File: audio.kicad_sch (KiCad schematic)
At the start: 18 parts, among them U13 CMM4030D, U15 MAX98357A

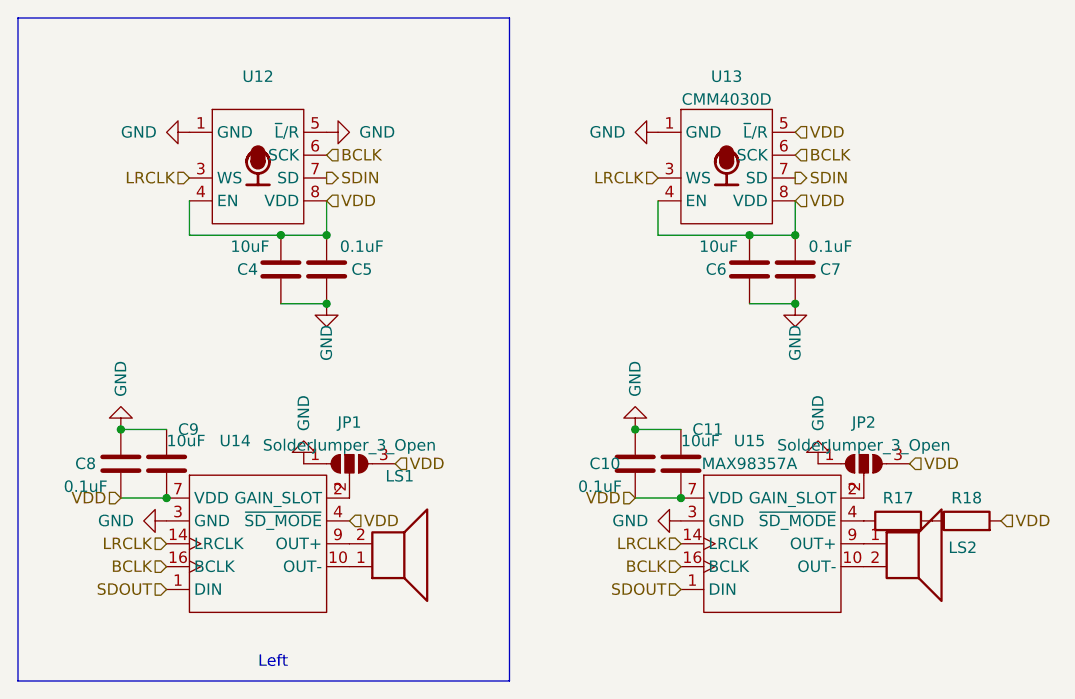
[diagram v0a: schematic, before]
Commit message: fully routed
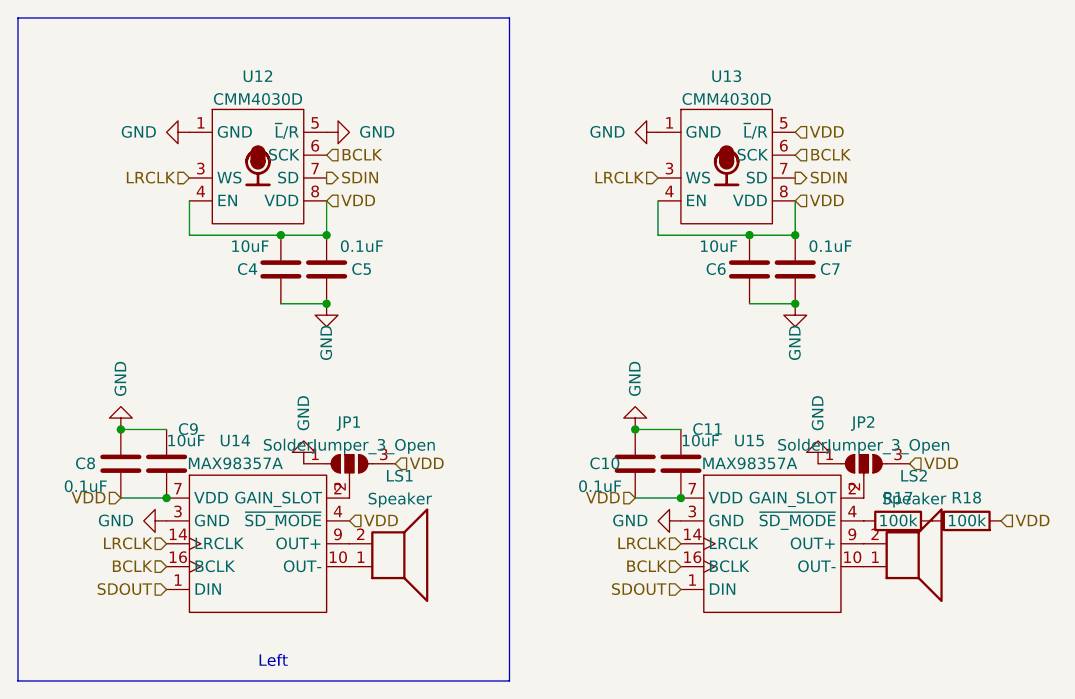
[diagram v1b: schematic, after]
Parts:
- JP1, JP2: footprint (none) -> Jumper:SolderJumper-3_P1.3mm_Open_RoundedPad1.0x1.5mm
- LS1, LS2: value (none) -> Speaker; footprint (none) -> misc:CMS1609
- R17, R18: value (none) -> 100k; footprint (none) -> Resistor_SMD:R_0603_1608Metric
- U12: value (none) -> CMM4030D
- U14: value (none) -> MAX98357A
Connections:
- net at LS2.1: now also U15.10 (OUT-); no longer U15.9 (OUT+)
- net at LS2.2: now also U15.9 (OUT+); no longer U15.10 (OUT-)
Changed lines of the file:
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@@
     (in_bom yes) (on_board yes)
     (property "Reference" "R18" (id 0) (at 127 77.47 90))
-    (property "Value" "" (id 1) (at 127 80.01 90))
-    (property "Footprint" "" (id 2) (at 127 81.788 90)
+    (property "Value" "100k" (id 1) (at 127 80.01 90))
+    (property "Footprint" "Resistor_SMD:R_0603_1608Metric" (id 2) (at 127 81.788 90)
       (effects (font (size 1.27 1.27)) hide)
     )
@@
     (in_bom yes) (on_board yes) (fields_autoplaced)
     (property "Reference" "LS1" (id 0) (at 64.008 75.0402 0))
-    (property "Value" "" (id 1) (at 64.008 77.5771 0))
-    (property "Footprint" "" (id 2) (at 63.5 80.01 0)
+    (property "Value" "Speaker" (id 1) (at 64.008 77.5771 0))
+    (property "Footprint" "misc:CMS1609" (id 2) (at 63.5 80.01 0)
       (effects (font (size 1.27 1.27)) hide)
     )
@@
     (property "Reference" "JP2" (id 0) (at 115.57 69.0712 0))
     (property "Value" "SolderJumper_3_Open" (id 1) (at 115.57 71.6081 0))
-    (property "Footprint" "" (id 2) (at 115.57 73.66 0)
+    (property "Footprint" "Jumper:SolderJumper-3_P1.3mm_Open_RoundedPad1.0x1.5mm" (id 2) (at 115.57 73.66 0)
       (effects (font (size 1.27 1.27)) hide)
     )
@@
     (pin "1")
   )
-  (symbol (lib_id "Device:Speaker") (at 120.65 82.55 0) (unit 1)
-    (in_bom yes) (on_board yes) (fields_autoplaced)
-    (property "Reference" "LS2" (id 0) (at 124.968 82.9853 0)
-      (effects (font (size 1.27 1.27)) (justify left))
-    )
-    (property "Value" "" (id 1) (at 124.968 85.5222 0)
-      (effects (font (size 1.27 1.27)) (justify left))
-    )
-    (property "Footprint" "" (id 2) (at 120.65 87.63 0)
+  (symbol (lib_id "Device:Speaker") (at 120.65 85.09 0) (mirror x) (unit 1)
+    (in_bom yes) (on_board yes) (fields_autoplaced)
+    (property "Reference" "LS2" (id 0) (at 121.158 75.0402 0))
+    (property "Value" "Speaker" (id 1) (at 121.158 77.5771 0))
+    (property "Footprint" "misc:CMS1609" (id 2) (at 120.65 80.01 0)
       (effects (font (size 1.27 1.27)) hide)
     )
@@
     (property "Reference" "JP1" (id 0) (at 58.42 69.0712 0))
     (property "Value" "SolderJumper_3_Open" (id 1) (at 58.42 71.6081 0))
-    (property "Footprint" "" (id 2) (at 58.42 73.66 0)
+    (property "Footprint" "Jumper:SolderJumper-3_P1.3mm_Open_RoundedPad1.0x1.5mm" (id 2) (at 58.42 73.66 0)
       (effects (font (size 1.27 1.27)) hide)
     )
@@
     (in_bom yes) (on_board yes) (fields_autoplaced)
     (property "Reference" "U12" (id 0) (at 48.26 30.641 0))
-    (property "Value" "" (id 1) (at 48.26 33.1779 0))
+    (property "Value" "CMM4030D" (id 1) (at 48.26 33.1779 0))
     (property "Footprint" "ic:CMM4030D_hand_solder" (id 2) (at 48.26 48.26 0)
       (effects (font (size 1.27 1.27)) hide)
@@
     (in_bom yes) (on_board yes)
     (property "Reference" "R17" (id 0) (at 119.38 77.47 90))
-    (property "Value" "" (id 1) (at 119.38 80.01 90))
-    (property "Footprint" "" (id 2) (at 119.38 81.788 90)
+    (property "Value" "100k" (id 1) (at 119.38 80.01 90))
+    (property "Footprint" "Resistor_SMD:R_0603_1608Metric" (id 2) (at 119.38 81.788 90)
       (effects (font (size 1.27 1.27)) hide)
     )
@@
     (in_bom yes) (on_board yes)
     (property "Reference" "U14" (id 0) (at 45.72 71.12 0))
-    (property "Value" "" (id 1) (at 45.72 73.66 0))
+    (property "Value" "MAX98357A" (id 1) (at 45.72 73.66 0))
     (property "Footprint" "Package_DFN_QFN:QFN-16-1EP_3x3mm_P0.5mm_EP1.45x1.45mm" (id 2) (at 48.26 95.25 0)
       (effects (font (size 1.27 1.27)) hide)
